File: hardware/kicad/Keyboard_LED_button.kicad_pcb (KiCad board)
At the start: 2 copper layers, 20 x 20 mm, 25 parts, among them J1 JST 4 Pin Qwiic I2C Connector, J2 JST 4 Pin Qwiic I2C Connector, J3 noknok_FlashPads_I2C-module, SW1 SW_Push, U1 CH32V003F4U6, U2 MT3540‑F23

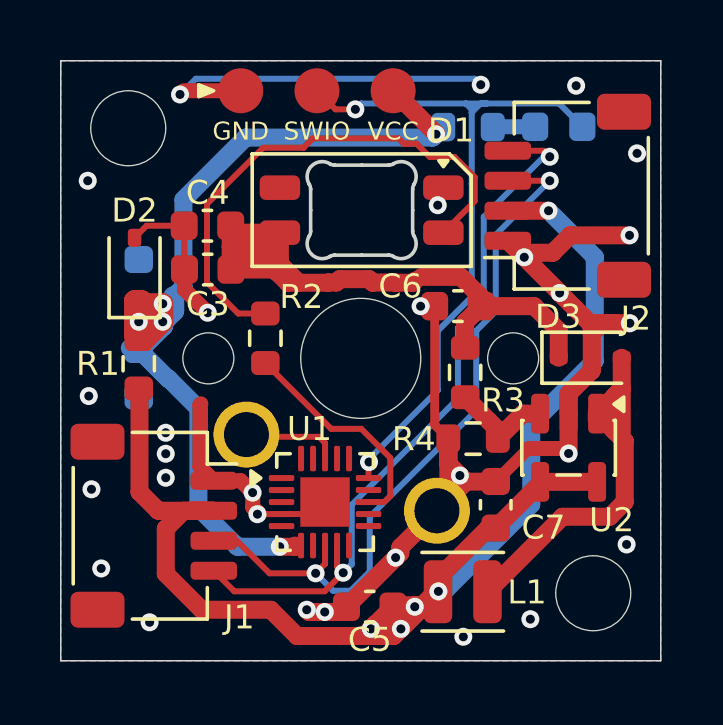
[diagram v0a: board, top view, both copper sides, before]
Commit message: hardware: update KiCad layout and schematic, consolidate schematic PDF and fix readme link
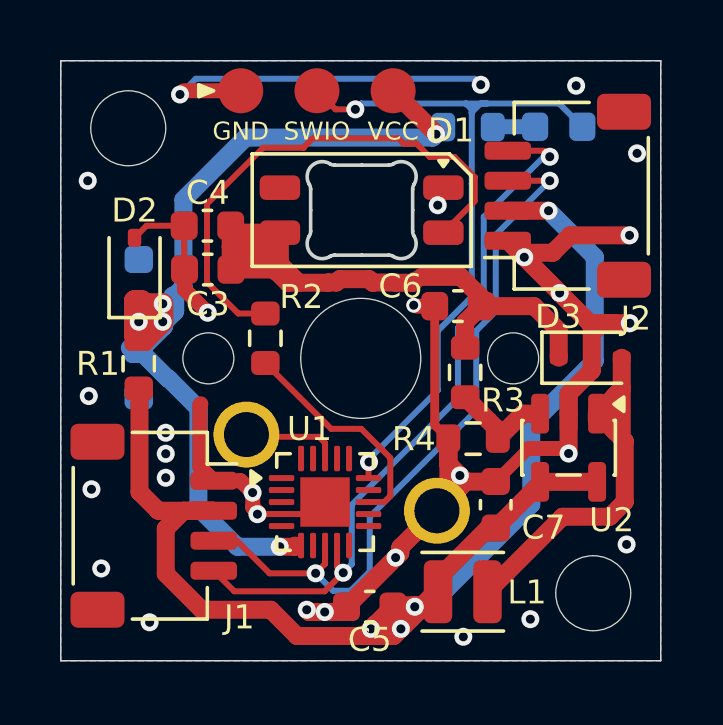
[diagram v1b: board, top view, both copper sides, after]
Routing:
- net +3.3V-IN: vias 5 -> 4
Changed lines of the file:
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@@
+	)
+	(segment
+		(start 131.878087 88.182557)
+		(end 132.462443 88.182557)
+		(width 0.5)
+		(layer "F.Cu")
+		(net "GND")
 	)
 	(segment
@@
 	)
 	(segment
-		(start 131.99529 88.182557)
-		(end 132.462443 88.182557)
-		(width 0.2)
-		(layer "F.Cu")
-		(net "GND")
-	)
-	(segment
 		(start 137.7 89.1)
 		(end 138.05 88.75)
@@
 	)
 	(segment
-		(start 132.462443 88.182557)
-		(end 132.465 88.18)
-		(width 0.2)
-		(layer "F.Cu")
-		(net "GND")
-	)
-	(segment
 		(start 127.36 95.11)
 		(end 128.41 95.11)
@@
 	)
 	(segment
+		(start 131.844843 88.149313)
+		(end 131.878087 88.182557)
+		(width 0.2)
+		(layer "F.Cu")
+		(net "GND")
+	)
+	(segment
 		(start 136.928091 91.100001)
 		(end 136.928091 91.7625)
@@
 		(net "GND")
 	)
+	(segment
+		(start 131.764841 88.149313)
+		(end 131.844843 88.149313)
+		(width 0.2)
+		(layer "F.Cu")
+		(net "GND")
+	)
 	(via
 		(at 135.45 86.55)
@@
 	)
 	(via
-		(at 131.99529 88.182557)
-		(size 0.6)
+		(at 131.764841 88.149313)
+		(size 0.5)
 		(drill 0.3)
 		(layers "F.Cu" "B.Cu")
@@
 		(net "+3.3V-IN")
 	)
-	(via
-		(at 132.5875 97.6875)
-		(size 0.6)
-		(drill 0.3)
-		(layers "F.Cu" "B.Cu")
-		(net "+3.3V-IN")
-	)
 	(segment
 		(start 137.8 86.54)
@@
 		(width 0.6)
 		(layer "F.Cu")
-		(net "+4.3V")
-	)
-	(segment
-		(start 131.157972 87.392043)
-		(end 131.165698 87.399769)
-		(width 0.6)
-		(layer "F.Cu")
